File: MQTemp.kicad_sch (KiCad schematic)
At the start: 7 parts, among them SW1 SW_DIP_x01, U1 WeMos_D1_mini, U2 DS18B20

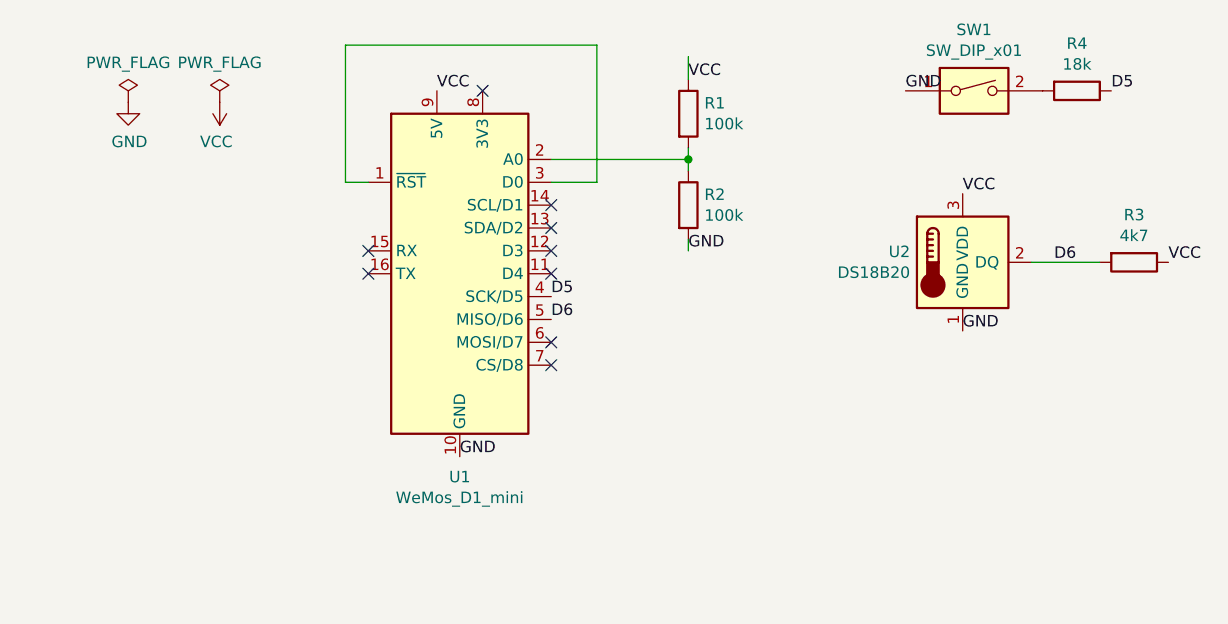
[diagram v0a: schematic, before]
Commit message: Added power connecter header holes
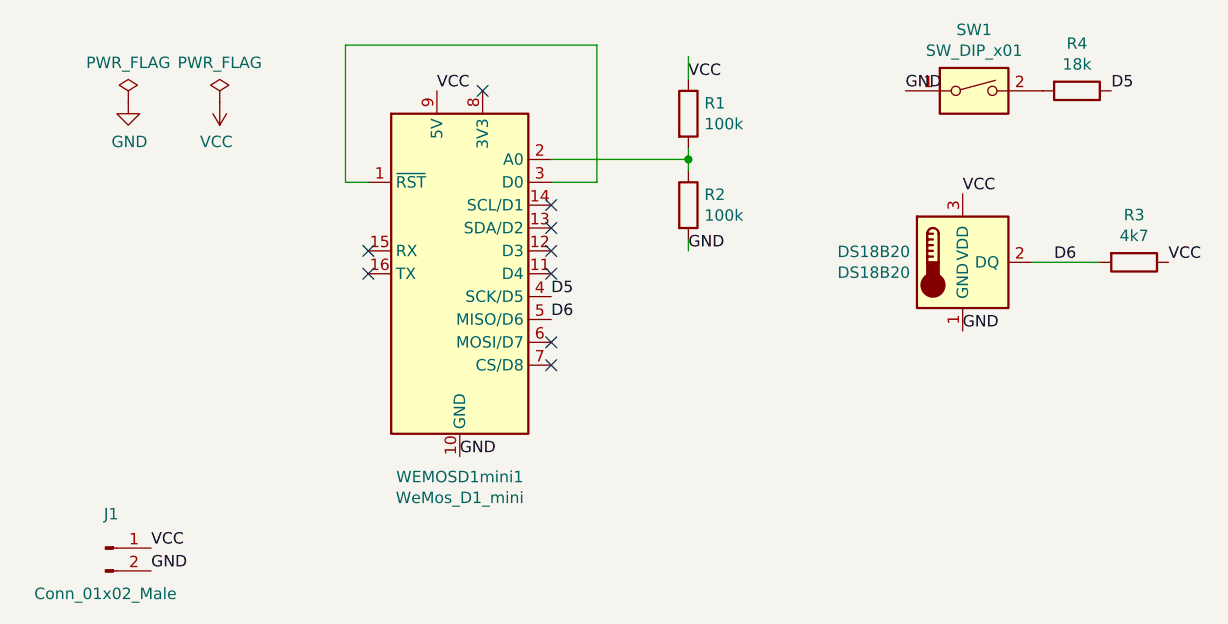
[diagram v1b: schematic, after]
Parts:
- added J1: Conn_01x02_Male, Connector_PinHeader_2.54mm:PinHeader_1x02_P2.54mm_Vertical, symbol Connector:Conn_01x02_Male
- renumbered U2 to DS18B20, U1 to WEMOSD1mini1
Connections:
- net GND: now also J1.2 (Pin_2)
- net VCC: now also J1.1 (Pin_1)
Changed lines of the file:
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@@
+    (effects (font (size 1.27 1.27)) (justify left bottom))
+  )
+  (label "GND" (at 27.94 76.2 0)
     (effects (font (size 1.27 1.27)) (justify left bottom))
   )
@@
   )
   (label "VCC" (at 59.69 22.86 0)
+    (effects (font (size 1.27 1.27)) (justify left bottom))
+  )
+  (label "VCC" (at 27.94 73.66 0)
     (effects (font (size 1.27 1.27)) (justify left bottom))
   )
@@
   (symbol (lib_id "MCU_Module:WeMos_D1_mini") (at 62.23 43.18 0) (unit 1)
     (in_bom yes) (on_board yes)
-    (property "Reference" "U1" (id 0) (at 62.23 65.7606 0))
+    (property "Reference" "WEMOSD1mini1" (id 0) (at 62.23 65.7606 0))
     (property "Value" "WeMos_D1_mini" (id 1) (at 62.23 68.072 0))
     (property "Footprint" "Module:WEMOS_D1_mini_light" (id 2) (at 62.23 72.39 0)
@@
   (symbol (lib_id "Sensor_Temperature:DS18B20") (at 118.11 41.91 0) (unit 1)
     (in_bom yes) (on_board yes)
-    (property "Reference" "U2" (id 0) (at 112.268 40.7416 0)
+    (property "Reference" "DS18B20" (id 0) (at 112.268 40.7416 0)
       (effects (font (size 1.27 1.27)) (justify right))
     )
@@
     (pin "2")
     (pin "3")
+  )
+  (symbol (lib_id "Connector:Conn_01x02_Male") (at 22.86 73.66 0) (unit 1)
+    (in_bom yes) (on_board yes)
+    (property "Reference" "J1" (id 0) (at 23.495 69.884 0))
+    (property "Value" "Conn_01x02_Male" (id 1) (at 22.86 78.74 0))
+    (property "Footprint" "Connector_PinHeader_2.54mm:PinHeader_1x02_P2.54mm_Vertical" (id 2) (at 22.86 73.66 0)
+      (effects (font (size 1.27 1.27)) hide)
+    )
+    (property "Datasheet" "~" (id 3) (at 22.86 73.66 0)
+      (effects (font (size 1.27 1.27)) hide)
+    )
+    (pin "1")
+    (pin "2")
   )
   (sheet_instances
@@
       (reference "#PWR0102") (unit 1) (value "VCC") (footprint "")
     )
+    (path "/00000000-0000-0000-0000-000062f533bf"
+      (reference "DS18B20") (unit 1) (value "DS18B20") (footprint "Package_TO_SOT_THT:TO-92_Inline")
+    )
+    (path "/53780b01-9002-4231-b325-caaeb774fd2a"
+      (reference "J1") (unit 1) (value "Conn_01x02_Male") (footprint "Connector_PinHeader_2.54mm:PinHeader_1x02_P2.54mm_Vertical")
+    )
     (path "/00000000-0000-0000-0000-000062f4efb9"
       (reference "R1") (unit 1) (value "100k") (footprint "Resistor_THT:R_Axial_DIN0309_L9.0mm_D3.2mm_P12.70mm_Horizontal")
@@
     )
     (path "/00000000-0000-0000-0000-000062f528bc"
-      (reference "U1") (unit 1) (value "WeMos_D1_mini") (footprint "Module:WEMOS_D1_mini_light")
-    )
-    (path "/00000000-0000-0000-0000-000062f533bf"
-      (reference "U2") (unit 1) (value "DS18B20") (footprint "Package_TO_SOT_THT:TO-92_Inline")
-    )
-  )
+      (reference "WEMOSD1mini1") (unit 1) (value "WeMos_D1_mini") (footprint "Module:WEMOS_D1_mini_light")
+    )
+  )

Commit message: Smaller footprints. More compact design
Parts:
- R1, R2, R3, R4: footprint Resistor_THT:R_Axial_DIN0309_L9.0mm_D3.2mm_P12.70mm_Horizontal -> Resistor_THT:R_Axial_DIN0207_L6.3mm_D2.5mm_P10.16mm_Horizontal
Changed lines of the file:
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@@
       (effects (font (size 1.27 1.27)) (justify left))
     )
-    (property "Footprint" "Resistor_THT:R_Axial_DIN0309_L9.0mm_D3.2mm_P12.70mm_Horizontal" (id 2) (at 85.852 25.4 90)
+    (property "Footprint" "Resistor_THT:R_Axial_DIN0207_L6.3mm_D2.5mm_P10.16mm_Horizontal" (id 2) (at 85.852 25.4 90)
       (effects (font (size 1.27 1.27)) hide)
     )
@@
       (effects (font (size 1.27 1.27)) (justify left))
     )
-    (property "Footprint" "Resistor_THT:R_Axial_DIN0309_L9.0mm_D3.2mm_P12.70mm_Horizontal" (id 2) (at 85.852 35.56 90)
+    (property "Footprint" "Resistor_THT:R_Axial_DIN0207_L6.3mm_D2.5mm_P10.16mm_Horizontal" (id 2) (at 85.852 35.56 90)
       (effects (font (size 1.27 1.27)) hide)
     )
@@
     (property "Reference" "R3" (id 0) (at 137.16 36.6522 90))
     (property "Value" "4k7" (id 1) (at 137.16 38.9636 90))
-    (property "Footprint" "Resistor_THT:R_Axial_DIN0309_L9.0mm_D3.2mm_P12.70mm_Horizontal" (id 2) (at 137.16 40.132 90)
+    (property "Footprint" "Resistor_THT:R_Axial_DIN0207_L6.3mm_D2.5mm_P10.16mm_Horizontal" (id 2) (at 137.16 40.132 90)
       (effects (font (size 1.27 1.27)) hide)
     )
@@
     (property "Reference" "R4" (id 0) (at 130.81 17.6022 90))
     (property "Value" "18k" (id 1) (at 130.81 19.9136 90))
-    (property "Footprint" "Resistor_THT:R_Axial_DIN0309_L9.0mm_D3.2mm_P12.70mm_Horizontal" (id 2) (at 130.81 21.082 90)
+    (property "Footprint" "Resistor_THT:R_Axial_DIN0207_L6.3mm_D2.5mm_P10.16mm_Horizontal" (id 2) (at 130.81 21.082 90)
       (effects (font (size 1.27 1.27)) hide)
     )
@@
     )
     (path "/00000000-0000-0000-0000-000062f4efb9"
-      (reference "R1") (unit 1) (value "100k") (footprint "Resistor_THT:R_Axial_DIN0309_L9.0mm_D3.2mm_P12.70mm_Horizontal")
+      (reference "R1") (unit 1) (value "100k") (footprint "Resistor_THT:R_Axial_DIN0207_L6.3mm_D2.5mm_P10.16mm_Horizontal")
     )
     (path "/00000000-0000-0000-0000-000062f508a0"
-      (reference "R2") (unit 1) (value "100k") (footprint "Resistor_THT:R_Axial_DIN0309_L9.0mm_D3.2mm_P12.70mm_Horizontal")
+      (reference "R2") (unit 1) (value "100k") (footprint "Resistor_THT:R_Axial_DIN0207_L6.3mm_D2.5mm_P10.16mm_Horizontal")
     )
     (path "/00000000-0000-0000-0000-000062f50d76"
-      (reference "R3") (unit 1) (value "4k7") (footprint "Resistor_THT:R_Axial_DIN0309_L9.0mm_D3.2mm_P12.70mm_Horizontal")
+      (reference "R3") (unit 1) (value "4k7") (footprint "Resistor_THT:R_Axial_DIN0207_L6.3mm_D2.5mm_P10.16mm_Horizontal")
     )
     (path "/00000000-0000-0000-0000-000062f51351"
-      (reference "R4") (unit 1) (value "18k") (footprint "Resistor_THT:R_Axial_DIN0309_L9.0mm_D3.2mm_P12.70mm_Horizontal")
+      (reference "R4") (unit 1) (value "18k") (footprint "Resistor_THT:R_Axial_DIN0207_L6.3mm_D2.5mm_P10.16mm_Horizontal")
     )
     (path "/00000000-0000-0000-0000-000062f51c54"
